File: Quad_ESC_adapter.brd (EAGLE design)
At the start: 101.6 x 41.1 mm, 14 parts, among them J1 284512-3, J2 284512-3, J3 284512-3, J4 284512-3

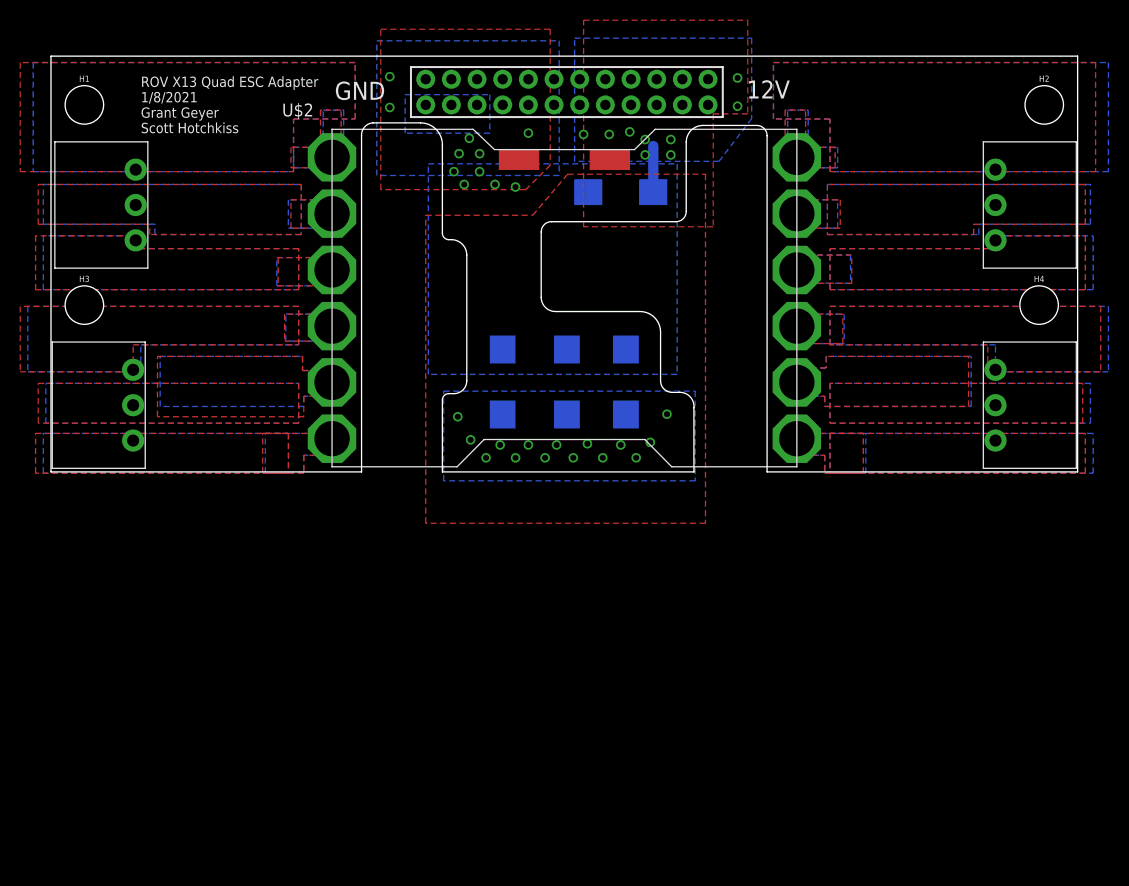
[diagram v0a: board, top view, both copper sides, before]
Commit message: Use aluminum caps for the adapter board
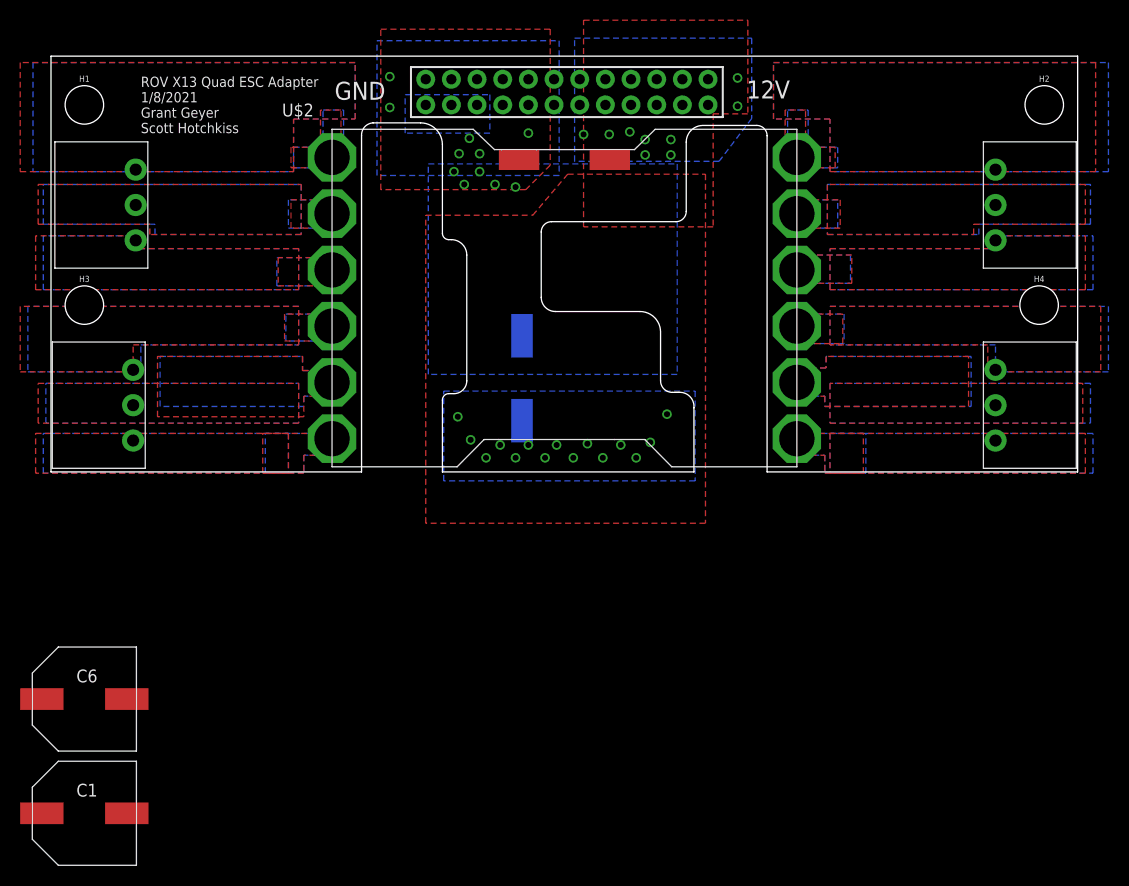
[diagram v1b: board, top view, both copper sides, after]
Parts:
- removed C2, C3, C4: 150uF, Tantalum Cap 150 uF - Kemet 2917 T491:2917(7343-31-METRIC)
- added C5, C6: 330uF, CAP, aluminin-capacitor-brick-UCM1H331MNL1GS:CAPAE1030X1050N
- C1: value 150uF -> 330uF; device Tantalum Cap 150 uF - Kemet 2917 T491:2917(7343-31-METRIC) -> CAP, aluminin-capacitor-brick-UCM1H331MNL1GS:CAPAE1030X1050N
- moved C1 59.5 mm to (-14.5, -33.8), flipped to the top, turned to 0 degrees
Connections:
- net 12V: now also C5.+, C6.+; no longer C2.+, C3.+, C4.+
- net GND: now also C5.-, C6.-; no longer C2.-, C3.-, C4.-
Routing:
- net 12V: track 4.57 -> 0.00 mm
